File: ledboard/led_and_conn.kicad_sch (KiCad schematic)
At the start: 29 parts, among them J2 Conn_02x20_Odd_Even, U3 TBD62083AFG, U4 TBD62083AFG, U5 TBD62783AFG

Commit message: 各種定数見直し,TPS2121の前後にデカップリングコンデンサを配置.
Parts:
- U3: MPN TBF62083AFG -> TBD62083AFG
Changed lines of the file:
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@@
-	)
-	(symbol
-		(lib_name "TBD62083AFG_1")
-		(lib_id "MyLib:TBD62083AFG")
-		(at 73.66 39.37 0)
-		(unit 1)
-		(exclude_from_sim no)
-		(in_bom yes)
-		(on_board yes)
-		(dnp no)
-		(fields_autoplaced yes)
-		(property "Reference" "U3"
-			(at 73.66 25.4 0)
-			(effects
-				(font
-					(size 1.524 1.524)
-				)
-			)
-		)
-		(property "Value" "TBD62083AFG"
-			(at 73.66 27.94 0)
-			(effects
-				(font
-					(size 1.524 1.524)
-				)
-			)
-		)
-		(property "Footprint" "MyLib:SOP18-P-375-1p27_TOS"
-			(at 74.168 60.96 0)
-			(effects
-				(font
-					(size 1.27 1.27)
-					(italic yes)
-				)
-				(hide yes)
-			)
-		)
-		(property "Datasheet" "https://toshiba.semicon-storage.com/info/docget.jsp?did=29808&prodName=TBD62083AFG"
-			(at 80.518 64.008 0)
-			(effects
-				(font
-					(size 1.27 1.27)
-					(italic yes)
-				)
-				(hide yes)
-			)
-		)
-		(property "Description" ""
-			(at 73.66 39.37 0)
-			(effects
-				(font
-					(size 1.27 1.27)
-				)
-				(hide yes)
-			)
-		)
-		(property "Manufacturer" "Toshiba"
-			(at 72.898 70.358 0)
-			(effects
-				(font
-					(size 1.27 1.27)
-				)
-				(hide yes)
-			)
-		)
-		(property "MPN" "TBF62083AFG"
-			(at 74.168 67.31 0)
-			(effects
-				(font
-					(size 1.27 1.27)
-				)
-				(hide yes)
-			)
-		)
-		(pin "6"
-		)
-		(pin "16"
-		)
-		(pin "14"
-		)
-		(pin "1"
-		)
-		(pin "9"
-		)
-		(pin "13"
-		)
-		(pin "8"
-		)
-		(pin "15"
-		)
-		(pin "18"
-		)
-		(pin "17"
-		)
-		(pin "5"
-		)
-		(pin "12"
-		)
-		(pin "10"
-		)
-		(pin "11"
-		)
-		(pin "4"
-		)
-		(pin "7"
-		)
-		(pin "2"
-		)
-		(pin "3"
-		)
-		(instances
-			(project "ledboard"
-				(path "/bdb2205c-1d8b-445a-876a-0efe4f06b647/49f30863-2902-4199-8294-8e718eb02f26"
-					(reference "U3")
-					(unit 1)
-				)
-			)
-		)
 	)
 	(symbol
@@
 					(unit 1)
 				)
+			)
+		)
+	)
+	(symbol
+		(lib_id "MyLib:TBD62083AFG")
+		(at 73.66 39.37 0)
+		(unit 1)
+		(exclude_from_sim no)
+		(in_bom yes)
+		(on_board yes)
+		(dnp no)
+		(fields_autoplaced yes)
+		(property "Reference" "U3"
+			(at 73.66 25.4 0)
+			(effects
+				(font
+					(size 1.524 1.524)
+				)
+			)
+		)
+		(property "Value" "TBD62083AFG"
+			(at 73.66 27.94 0)
+			(effects
+				(font
+					(size 1.524 1.524)
+				)
+			)
+		)
+		(property "Footprint" "MyLib:SOP18-P-375-1p27_TOS"
+			(at 74.168 60.96 0)
+			(effects
+				(font
+					(size 1.27 1.27)
+					(italic yes)
+				)
+				(hide yes)
+			)
+		)
+		(property "Datasheet" "https://toshiba.semicon-storage.com/info/docget.jsp?did=29808&prodName=TBD62083AFG"
+			(at 80.518 64.008 0)
+			(effects
+				(font
+					(size 1.27 1.27)
+					(italic yes)
+				)
+				(hide yes)
+			)
+		)
+		(property "Description" ""
+			(at 73.66 39.37 0)
+			(effects
+				(font
+					(size 1.27 1.27)
+				)
+				(hide yes)
+			)
+		)
+		(property "Manufacturer" "Toshiba"
+			(at 72.898 70.358 0)
+			(effects
+				(font
+					(size 1.27 1.27)
+				)
+				(hide yes)
+			)
+		)
+		(property "MPN" "TBD62083AFG"
+			(at 74.168 67.31 0)
+			(effects
+				(font
+					(size 1.27 1.27)
+				)
+				(hide yes)
+			)
+		)
+		(pin "7"
+		)
+		(pin "10"
+		)
+		(pin "15"
+		)
+		(pin "2"
+		)
+		(pin "1"
+		)
+		(pin "3"
+		)
+		(pin "17"
+		)
+		(pin "12"
+		)
+		(pin "13"
+		)
+		(pin "8"
+		)
+		(pin "9"
+		)
+		(pin "18"
+		)
+		(pin "11"
+		)
+		(pin "5"
+		)
+		(pin "6"
+		)
+		(pin "4"
+		)
+		(pin "14"
+		)
+		(pin "16"
+		)
+		(instances
+			(project "ledboard"
+				(path "/bdb2205c-1d8b-445a-876a-0efe4f06b647/49f30863-2902-4199-8294-8e718eb02f26"
+					(reference "U3")
+					(unit 1)
+				)

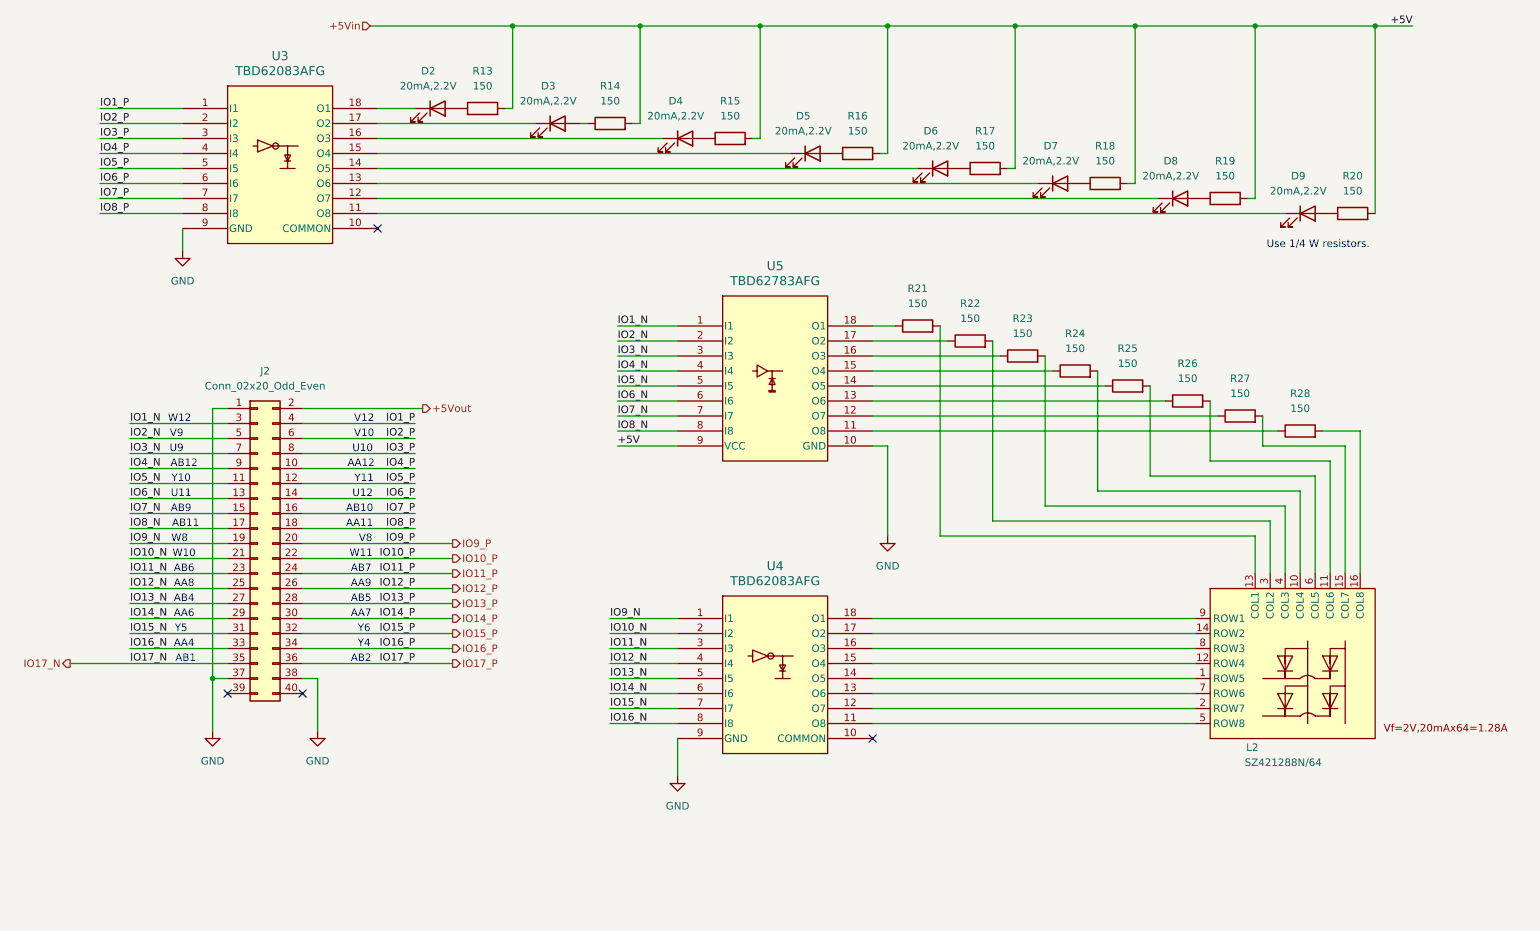
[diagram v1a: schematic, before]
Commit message: 部品の再アノテーションを行う.
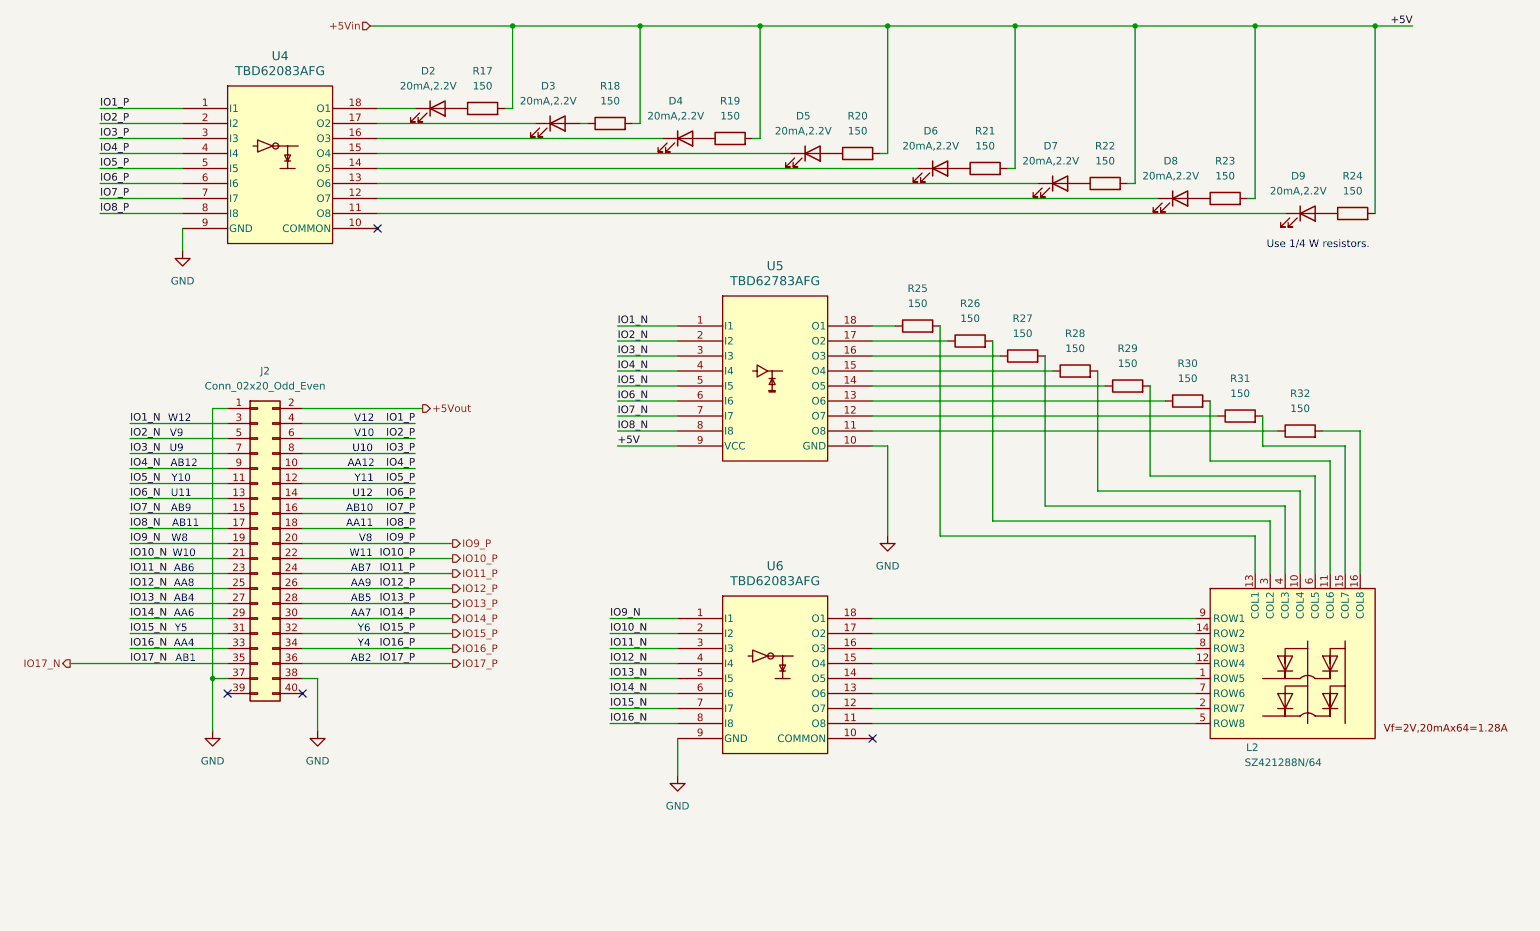
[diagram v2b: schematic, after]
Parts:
- renumbered R13 to R17, R14 to R18, R15 to R19, R16 to R20, R17 to R21, R18 to R22, R19 to R23, R20 to R24, R21 to R25, R22 to R26, R23 to R27, R24 to R28, R25 to R29, R26 to R30, R27 to R31, R28 to R32, U3 to U4, U4 to U6
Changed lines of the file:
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@@
 		(dnp no)
 		(fields_autoplaced yes)
-		(property "Reference" "R13"
+		(property "Reference" "R17"
 			(at 107.95 27.94 90)
 			(effects
@@
 			(project "ledboard"
 				(path "/bdb2205c-1d8b-445a-876a-0efe4f06b647/49f30863-2902-4199-8294-8e718eb02f26"
-					(reference "R13")
+					(reference "R17")
 					(unit 1)
 				)
@@
 		(dnp no)
 		(fields_autoplaced yes)
-		(property "Reference" "R22"
+		(property "Reference" "R26"
 			(at 190.5 67.31 90)
 			(effects
@@
 			(project "ledboard"
 				(path "/bdb2205c-1d8b-445a-876a-0efe4f06b647/49f30863-2902-4199-8294-8e718eb02f26"
-					(reference "R22")
+					(reference "R26")
 					(unit 1)
 				)
@@
 		(dnp no)
 		(fields_autoplaced yes)
-		(property "Reference" "R15"
+		(property "Reference" "R19"
 			(at 149.86 33.02 90)
 			(effects
@@
 			(project "ledboard"
 				(path "/bdb2205c-1d8b-445a-876a-0efe4f06b647/49f30863-2902-4199-8294-8e718eb02f26"
-					(reference "R15")
+					(reference "R19")
 					(unit 1)
 				)
@@
 		(on_board yes)
 		(dnp no)
-		(property "Reference" "#PWR015"
+		(property "Reference" "#PWR014"
 			(at 176.53 113.03 0)
 			(effects
@@
 			(project "ledboard"
 				(path "/bdb2205c-1d8b-445a-876a-0efe4f06b647/49f30863-2902-4199-8294-8e718eb02f26"
-					(reference "#PWR015")
+					(reference "#PWR014")
 					(unit 1)
 				)
@@
 		(dnp no)
 		(fields_autoplaced yes)
-		(property "Reference" "R14"
+		(property "Reference" "R18"
 			(at 129.54 30.48 90)
 			(effects
@@
 			(project "ledboard"
 				(path "/bdb2205c-1d8b-445a-876a-0efe4f06b647/49f30863-2902-4199-8294-8e718eb02f26"
-					(reference "R14")
+					(reference "R18")
 					(unit 1)
 				)
@@
 		(dnp no)
 		(fields_autoplaced yes)
-		(property "Reference" "R23"
+		(property "Reference" "R27"
 			(at 199.39 69.85 90)
 			(effects
@@
 			(project "ledboard"
 				(path "/bdb2205c-1d8b-445a-876a-0efe4f06b647/49f30863-2902-4199-8294-8e718eb02f26"
-					(reference "R23")
+					(reference "R27")
 					(unit 1)
 				)
@@
 		(on_board yes)
 		(dnp no)
-		(property "Reference" "R18"
+		(property "Reference" "R22"
 			(at 213.36 40.64 90)
 			(effects
@@
 			(project "ledboard"
 				(path "/bdb2205c-1d8b-445a-876a-0efe4f06b647/49f30863-2902-4199-8294-8e718eb02f26"
-					(reference "R18")
+					(reference "R22")
 					(unit 1)
 				)
@@
 		(dnp no)
 		(fields_autoplaced yes)
-		(property "Reference" "U4"
+		(property "Reference" "U6"
 			(at 157.48 111.76 0)
 			(effects
@@
 			(project "ledboard"
 				(path "/bdb2205c-1d8b-445a-876a-0efe4f06b647/49f30863-2902-4199-8294-8e718eb02f26"
-					(reference "U4")
+					(reference "U6")
 					(unit 1)
 				)
@@
 		(dnp no)
 		(fields_autoplaced yes)
-		(property "Reference" "#PWR011"
+		(property "Reference" "#PWR015"
 			(at 62.23 146.05 0)
 			(effects
@@
 			(project "ledboard"
 				(path "/bdb2205c-1d8b-445a-876a-0efe4f06b647/49f30863-2902-4199-8294-8e718eb02f26"
-					(reference "#PWR011")
+					(reference "#PWR015")
 					(unit 1)
 				)
@@
 		(dnp no)
 		(fields_autoplaced yes)
-		(property "Reference" "R26"
+		(property "Reference" "R30"
 			(at 227.33 77.47 90)
 			(effects
@@
 			(project "ledboard"
 				(path "/bdb2205c-1d8b-445a-876a-0efe4f06b647/49f30863-2902-4199-8294-8e718eb02f26"
-					(reference "R26")
+					(reference "R30")
 					(unit 1)
 				)
@@
 		(dnp no)
 		(fields_autoplaced yes)
-		(property "Reference" "R21"
+		(property "Reference" "R25"
 			(at 181.61 64.77 90)
 			(effects
@@
 			(project "ledboard"
 				(path "/bdb2205c-1d8b-445a-876a-0efe4f06b647/49f30863-2902-4199-8294-8e718eb02f26"
-					(reference "R21")
+					(reference "R25")
 					(unit 1)
 				)
@@
 		(dnp no)
 		(fields_autoplaced yes)
-		(property "Reference" "R19"
+		(property "Reference" "R23"
 			(at 233.68 43.18 90)
 			(effects
@@
 			(project "ledboard"
 				(path "/bdb2205c-1d8b-445a-876a-0efe4f06b647/49f30863-2902-4199-8294-8e718eb02f26"
-					(reference "R19")
+					(reference "R23")
 					(unit 1)
 				)
@@
 		(dnp no)
 		(fields_autoplaced yes)
-		(property "Reference" "#PWR012"
+		(property "Reference" "#PWR016"
 			(at 80.01 146.05 0)
 			(effects
@@
 			(project "ledboard"
 				(path "/bdb2205c-1d8b-445a-876a-0efe4f06b647/49f30863-2902-4199-8294-8e718eb02f26"
-					(reference "#PWR012")
+					(reference "#PWR016")
 					(unit 1)
 				)
@@
 		(dnp no)
 		(fields_autoplaced yes)
-		(property "Reference" "R20"
+		(property "Reference" "R24"
 			(at 255.27 45.72 90)
 			(effects
@@
 			(project "ledboard"
 				(path "/bdb2205c-1d8b-445a-876a-0efe4f06b647/49f30863-2902-4199-8294-8e718eb02f26"
-					(reference "R20")
+					(reference "R24")
 					(unit 1)
 				)
@@
 		(dnp no)
 		(fields_autoplaced yes)
-		(property "Reference" "R24"
+		(property "Reference" "R28"
 			(at 208.28 72.39 90)
 			(effects
@@
 			(project "ledboard"
 				(path "/bdb2205c-1d8b-445a-876a-0efe4f06b647/49f30863-2902-4199-8294-8e718eb02f26"
-					(reference "R24")
+					(reference "R28")
 					(unit 1)
 				)
@@
 		(dnp no)
 		(fields_autoplaced yes)
-		(property "Reference" "R28"
+		(property "Reference" "R32"
 			(at 246.38 82.55 90)
 			(effects
@@
 			(project "ledboard"
 				(path "/bdb2205c-1d8b-445a-876a-0efe4f06b647/49f30863-2902-4199-8294-8e718eb02f26"
-					(reference "R28")
+					(reference "R32")
 					(unit 1)
 				)
@@
 		(dnp no)
 		(fields_autoplaced yes)
-		(property "Reference" "R25"
+		(property "Reference" "R29"
 			(at 217.17 74.93 90)
 			(effects
@@
 			(project "ledboard"
 				(path "/bdb2205c-1d8b-445a-876a-0efe4f06b647/49f30863-2902-4199-8294-8e718eb02f26"
-					(reference "R25")
+					(reference "R29")
 					(unit 1)
 				)
@@
 		(dnp no)
 		(fields_autoplaced yes)
-		(property "Reference" "R17"
+		(property "Reference" "R21"
 			(at 193.04 38.1 90)
 			(effects
@@
 			(project "ledboard"
 				(path "/bdb2205c-1d8b-445a-876a-0efe4f06b647/49f30863-2902-4199-8294-8e718eb02f26"
-					(reference "R17")
+					(reference "R21")
 					(unit 1)
 				)
@@
 		(dnp no)
 		(fields_autoplaced yes)
-		(property "Reference" "R27"
+		(property "Reference" "R31"
 			(at 236.22 80.01 90)
 			(effects
@@
 			(project "ledboard"
 				(path "/bdb2205c-1d8b-445a-876a-0efe4f06b647/49f30863-2902-4199-8294-8e718eb02f26"
-					(reference "R27")
+					(reference "R31")
 					(unit 1)
 				)
@@
 		(dnp no)
 		(fields_autoplaced yes)
-		(property "Reference" "R16"
+		(property "Reference" "R20"
 			(at 171.45 35.56 90)
 			(effects
@@
 			(project "ledboard"
 				(path "/bdb2205c-1d8b-445a-876a-0efe4f06b647/49f30863-2902-4199-8294-8e718eb02f26"
-					(reference "R16")
+					(reference "R20")
 					(unit 1)
 				)
@@
 		(dnp no)
 		(fields_autoplaced yes)
-		(property "Reference" "U3"
+		(property "Reference" "U4"
 			(at 73.66 25.4 0)
 			(effects
@@
 			(project "ledboard"
 				(path "/bdb2205c-1d8b-445a-876a-0efe4f06b647/49f30863-2902-4199-8294-8e718eb02f26"
-					(reference "U3")
-					(unit 1)
-				)
+					(reference "U4")
+					(unit 1)
+				)

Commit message: 部品が決まったので,コミットします.
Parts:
- D10: renamed from L2; footprint (none) -> MyLib:SZ421288N_64
- D2, D3, D4, D5, D6, D7, D8, D9: footprint LED_SMD:LED_0402_1005Metric -> LED_SMD:LED_0603_1608Metric; MPN (none) -> SML-D12V8W(C); Manufacturer (none) -> ROHM
- J2: footprint (none) -> Connector_PinSocket_2.54mm:PinSocket_2x20_P2.54mm_Vertical; MPN (none) -> DS1023-2 20SF11; Manufacturer (none) -> CONNFLY
- R17, R18: footprint Resistor_SMD:R_0402_1005Metric -> Resistor_SMD:R_0603_1608Metric; MPN (none) -> SR0603FR-7T150RL; Manufacturer (none) -> YAGEO
- R19, R20, R21, R22, R23, R24, R25, R26, R27, R28, R29, R30, R31, R32: footprint (none) -> Resistor_SMD:R_0603_1608Metric; MPN (none) -> SR0603FR-7T150RL; Manufacturer (none) -> YAGEO
- U5: MPN (none) -> TBD62783AFG; Manufacturer (none) -> Toshiba
- U6: MPN TBF62083AFG -> TBD62083AFG
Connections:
- net +5Vin renamed +5V_VCC
- net +5Vout renamed +5V
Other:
- note added: "LED and Connector"

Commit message: ERC解消まで.
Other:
- moved on the sheet: D10

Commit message: LOGとボード名を追加します.
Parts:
- D2, D3, D4, D5, D6, D7, D8, D9: MPN SML-D12V8W(C) -> SML-D12V8WC
- J2: MPN DS1023-2 20SF11 -> DS1023-2*20SF11
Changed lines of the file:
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@@
 			)
 		)
-		(property "Datasheet" "~"
+		(property "Datasheet" "https://fscdn.rohm.com/jp/products/databook/datasheet/opto/led/chip_mono/sml-d12v8wt86(c)-j.pdf"
 			(at 163.83 41.91 0)
 			(effects
@@
 			)
 		)
-		(property "MPN" "SML-D12V8W(C)"
+		(property "MPN" "SML-D12V8WC"
 			(at 163.83 41.91 0)
 			(effects
@@
 			)
 		)
-		(property "Datasheet" "~"
+		(property "Datasheet" "https://fscdn.rohm.com/jp/products/databook/datasheet/opto/led/chip_mono/sml-d12v8wt86(c)-j.pdf"
 			(at 120.65 36.83 0)
 			(effects
@@
 			)
 		)
-		(property "MPN" "SML-D12V8W(C)"
+		(property "MPN" "SML-D12V8WC"
 			(at 120.65 36.83 0)
 			(effects
@@
 			)
 		)
-		(property "Datasheet" "~"
+		(property "Datasheet" "https://fscdn.rohm.com/jp/products/databook/datasheet/opto/led/chip_mono/sml-d12v8wt86(c)-j.pdf"
 			(at 142.24 39.37 0)
 			(effects
@@
 			)
 		)
-		(property "MPN" "SML-D12V8W(C)"
+		(property "MPN" "SML-D12V8WC"
 			(at 142.24 39.37 0)
 			(effects
@@
 			)
 		)
-		(property "MPN" "DS1023-2 20SF11"
+		(property "MPN" "DS1023-2*20SF11"
 			(at 69.85 107.95 0)
 			(effects
@@
 			)
 		)
-		(property "Datasheet" "~"
+		(property "Datasheet" "https://fscdn.rohm.com/jp/products/databook/datasheet/opto/led/chip_mono/sml-d12v8wt86(c)-j.pdf"
 			(at 100.33 34.29 0)
 			(effects
@@
 			)
 		)
-		(property "MPN" "SML-D12V8W(C)"
+		(property "MPN" "SML-D12V8WC"
 			(at 100.33 34.29 0)
 			(effects
@@
 			)
 		)
-		(property "Datasheet" "~"
+		(property "Datasheet" "https://fscdn.rohm.com/jp/products/databook/datasheet/opto/led/chip_mono/sml-d12v8wt86(c)-j.pdf"
 			(at 205.74 46.99 0)
 			(effects
@@
 			)
 		)
-		(property "MPN" "SML-D12V8W(C)"
+		(property "MPN" "SML-D12V8WC"
 			(at 205.74 46.99 0)
 			(effects
@@
 			)
 		)
-		(property "Datasheet" "~"
+		(property "Datasheet" "https://fscdn.rohm.com/jp/products/databook/datasheet/opto/led/chip_mono/sml-d12v8wt86(c)-j.pdf"
 			(at 226.06 49.53 0)
 			(effects
@@
 			)
 		)
-		(property "MPN" "SML-D12V8W(C)"
+		(property "MPN" "SML-D12V8WC"
 			(at 226.06 49.53 0)
 			(effects
@@
 			)
 		)
-		(property "Datasheet" "~"
+		(property "Datasheet" "https://fscdn.rohm.com/jp/products/databook/datasheet/opto/led/chip_mono/sml-d12v8wt86(c)-j.pdf"
 			(at 247.65 52.07 0)
 			(effects
@@
 			)
 		)
-		(property "MPN" "SML-D12V8W(C)"
+		(property "MPN" "SML-D12V8WC"
 			(at 247.65 52.07 0)
 			(effects
@@
 			)
 		)
-		(property "Datasheet" "~"
+		(property "Datasheet" "https://fscdn.rohm.com/jp/products/databook/datasheet/opto/led/chip_mono/sml-d12v8wt86(c)-j.pdf"
 			(at 185.42 44.45 0)
 			(effects
@@
 			)
 		)
-		(property "MPN" "SML-D12V8W(C)"
+		(property "MPN" "SML-D12V8WC"
 			(at 185.42 44.45 0)
 			(effects

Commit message: 部品変更とアートワークの修正.
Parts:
- D2, D3, D4, D5, D6, D7, D8, D9: MPN SML-D12V8WC -> SML-D12V8WT86C
- J2: value Conn_02x20_Odd_Even -> DS1023-2*20SF11
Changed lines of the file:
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@@
 			)
 		)
-		(property "MPN" "SML-D12V8WC"
+		(property "MPN" "SML-D12V8WT86C"
 			(at 163.83 41.91 0)
 			(effects
@@
 			)
 		)
-		(property "MPN" "SML-D12V8WC"
+		(property "MPN" "SML-D12V8WT86C"
 			(at 120.65 36.83 0)
 			(effects
@@
 			)
 		)
-		(property "MPN" "SML-D12V8WC"
+		(property "MPN" "SML-D12V8WT86C"
 			(at 142.24 39.37 0)
 			(effects
@@
 		(on_board yes)
 		(dnp no)
-		(fields_autoplaced yes)
 		(property "Reference" "J2"
 			(at 71.12 78.74 0)
@@
 			)
 		)
-		(property "Value" "Conn_02x20_Odd_Even"
+		(property "Value" "DS1023-2*20SF11"
 			(at 71.12 81.28 0)
 			(effects
@@
 			)
 		)
-		(property "MPN" "SML-D12V8WC"
+		(property "MPN" "SML-D12V8WT86C"
 			(at 100.33 34.29 0)
 			(effects
@@
 			)
 		)
-		(property "MPN" "SML-D12V8WC"
+		(property "MPN" "SML-D12V8WT86C"
 			(at 205.74 46.99 0)
 			(effects
@@
 			)
 		)
-		(property "MPN" "SML-D12V8WC"
+		(property "MPN" "SML-D12V8WT86C"
 			(at 226.06 49.53 0)
 			(effects
@@
 			)
 		)
-		(property "MPN" "SML-D12V8WC"
+		(property "MPN" "SML-D12V8WT86C"
 			(at 247.65 52.07 0)
 			(effects
@@
 			)
 		)
-		(property "MPN" "SML-D12V8WC"
+		(property "MPN" "SML-D12V8WT86C"
 			(at 185.42 44.45 0)
 			(effects

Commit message: LSCS品番を追加. コンデンサの品番を変更します.
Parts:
- D10: LCSC Part # (none) -> C2980922
- D2, D3, D4, D5, D6, D7, D8, D9: LCSC Part # (none) -> C458032
- J2: LCSC Part # (none) -> C132132
- R17, R18, R19, R20, R21, R22, R23, R24, R25, R26, R27, R28, R29, R30, R31, R32: LCSC Part # (none) -> C873675
- U4, U6: LCSC Part # (none) -> C163228
- U5: LCSC Part # (none) -> C97745
